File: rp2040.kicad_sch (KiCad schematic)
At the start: 28 parts, among them J1 Conn_ARM_SWD_TagConnect_TC203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, SW1 boot, SW2 reset, U1 LM4040DBZ-3, U2 W25Q128JVS, U3 RP2040, Y1 NX3225GA

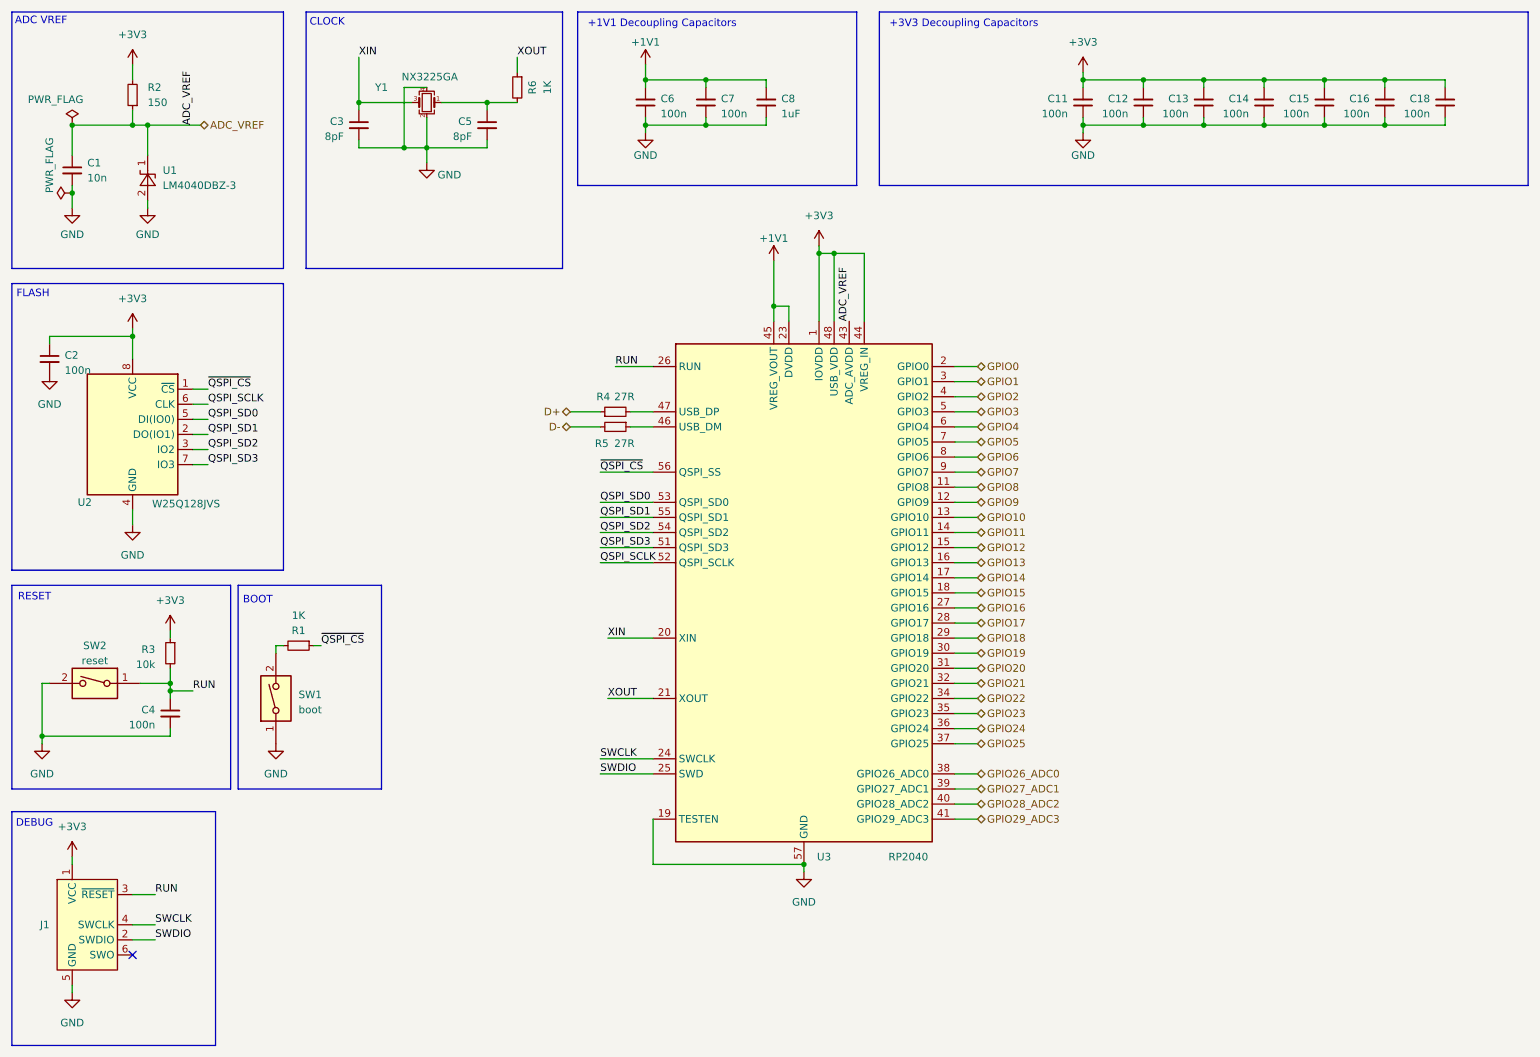
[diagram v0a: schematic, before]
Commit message: layout from scratch, change some components to basic JLCPCB parts
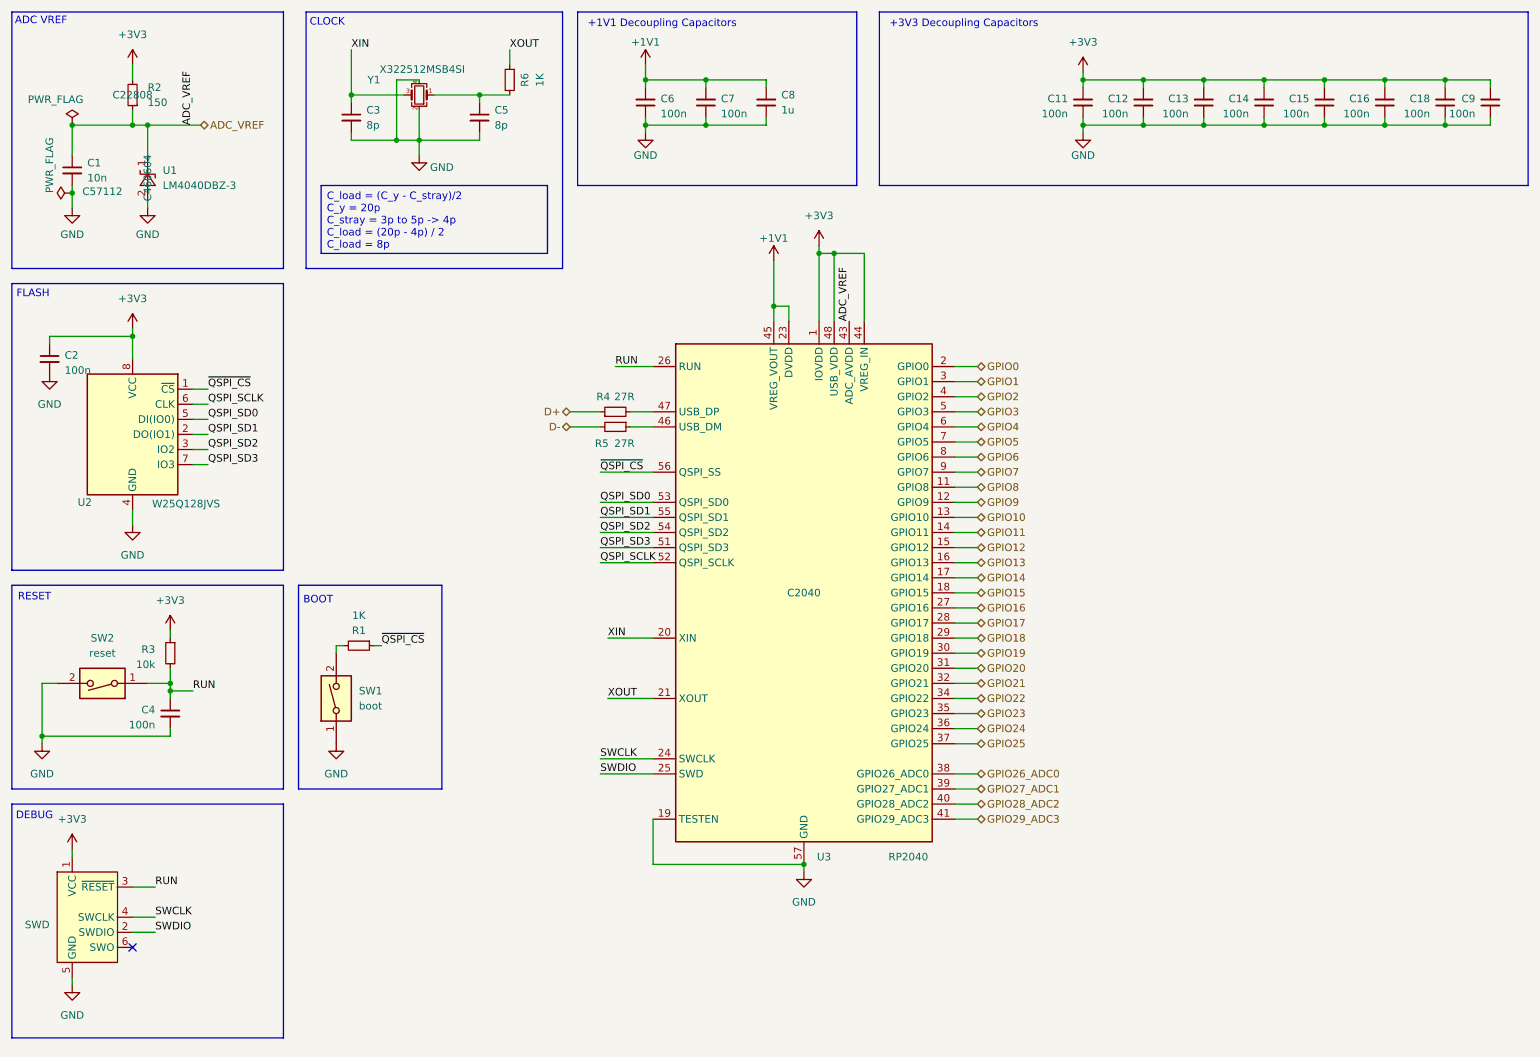
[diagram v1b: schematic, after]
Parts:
- added C9: 100n, Capacitor_SMD:C_0402_1005Metric_Pad0.74x0.62mm_HandSolder, symbol Device:C_Small
- C1: LCSC Part# (none) -> C57112
- C11, C12, C13, C14, C15, C16, C18, C2, C4, C6, C7: LCSC Part# C41851 -> C307331
- C3, C5: value 8pF -> 8p
- C8: value 1uF -> 1u; LCSC Part# C87143 -> C52923
- J1: value Conn_ARM_SWD_TagConnect_TC2030-NL -> SWD
- R1, R6: LCSC Part# C226166 -> C11702
- R2: LCSC Part# (none) -> C22808
- R3: LCSC Part# C60490 -> C25744
- R4, R5: LCSC Part# C2909343 -> C140174
- SW1, SW2: footprint Button_Switch_SMD:SW_SPST_B3U-1000P -> Button_Switch_SMD:SW_Push_1P1T_XKB_TS-1187A; LCSC Part# C115357 -> C318884
- U1: LCSC Part# (none) -> C460604
- U2: footprint Package_SO:SOIC-8_5.23x5.23mm_P1.27mm -> Package_SON:WSON-8-1EP_6x5mm_P1.27mm_EP3.4x4.3mm; LCSC Part# (none) -> C190862
- U3: LCSC Part# (none) -> C2040
- Y1: value NX3225GA -> X322512MSB4SI; LCSC Part# C481407 -> C9002
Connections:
- net +3V3: now also C9.2
- net GND: now also C9.1
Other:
- moved on the sheet: C3, C5, R1, R6, Y1
